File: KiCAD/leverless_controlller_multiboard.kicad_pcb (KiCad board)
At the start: 2 copper layers, 210 x 130 mm, 67 parts, among them J1 USB_C_Receptacle_USB2.0_14P, J2 Conn_01x03_Socket, SW1 Memory Reset, SW10_SHARE1 SW_Push, SW11_START1 SW_Push, SW12_THROW1 SW_Push, SW14_PS1 SW_Push, SW15_TOUCHPAD1 SW_Push, SW16_SPACE1 SW_Push, SW17_W1 SW_Push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

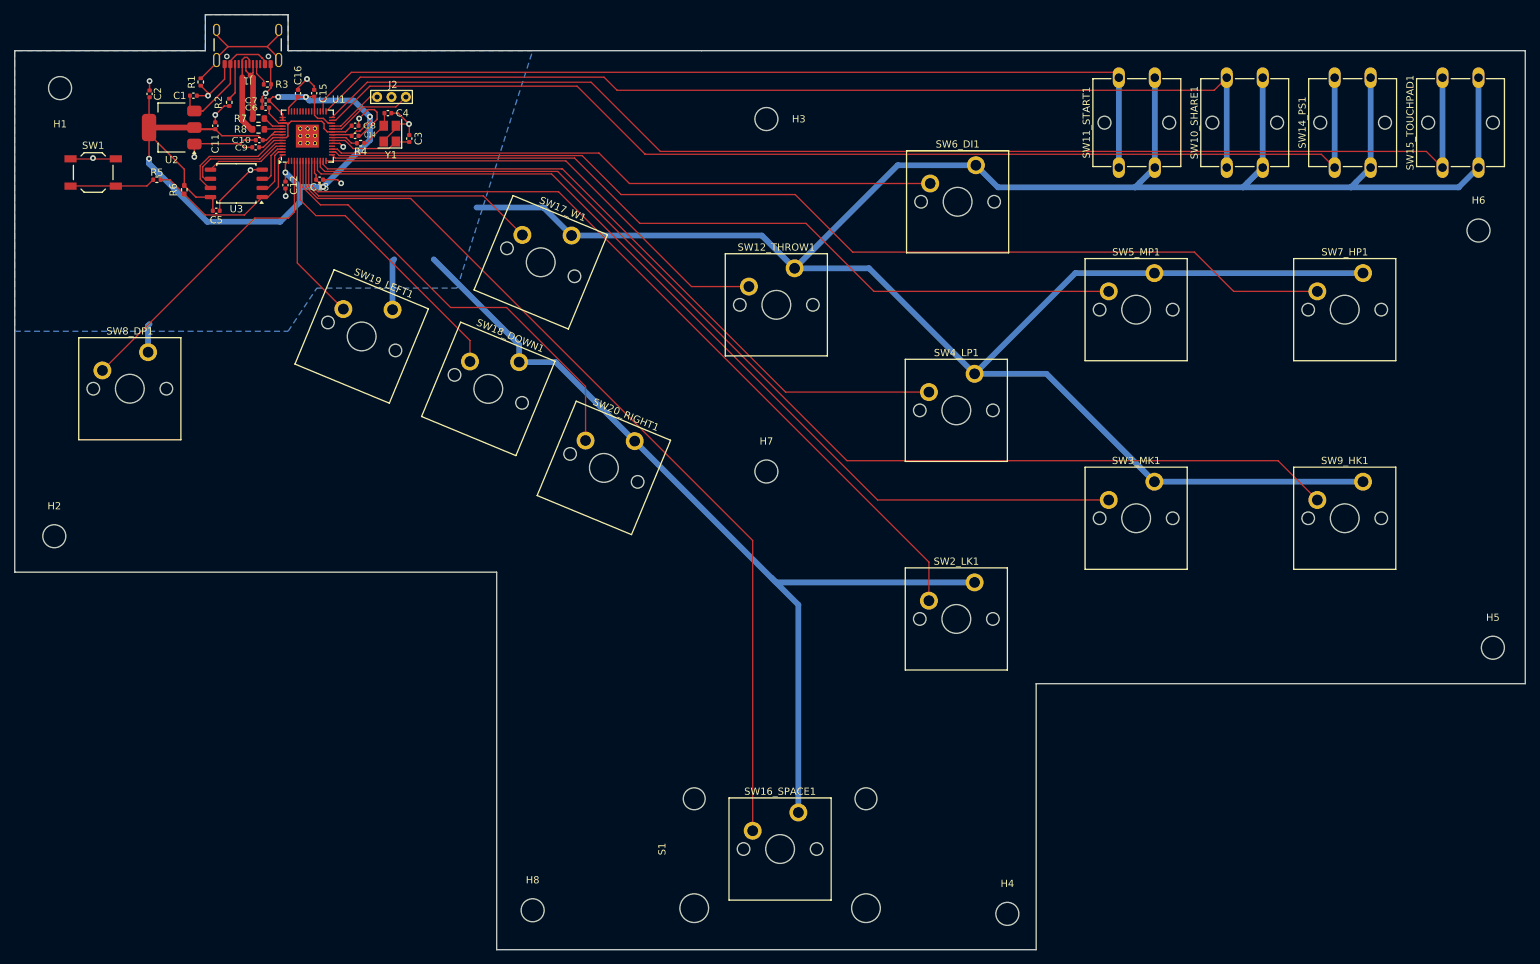
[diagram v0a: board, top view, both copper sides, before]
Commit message: Add multiboard configurations
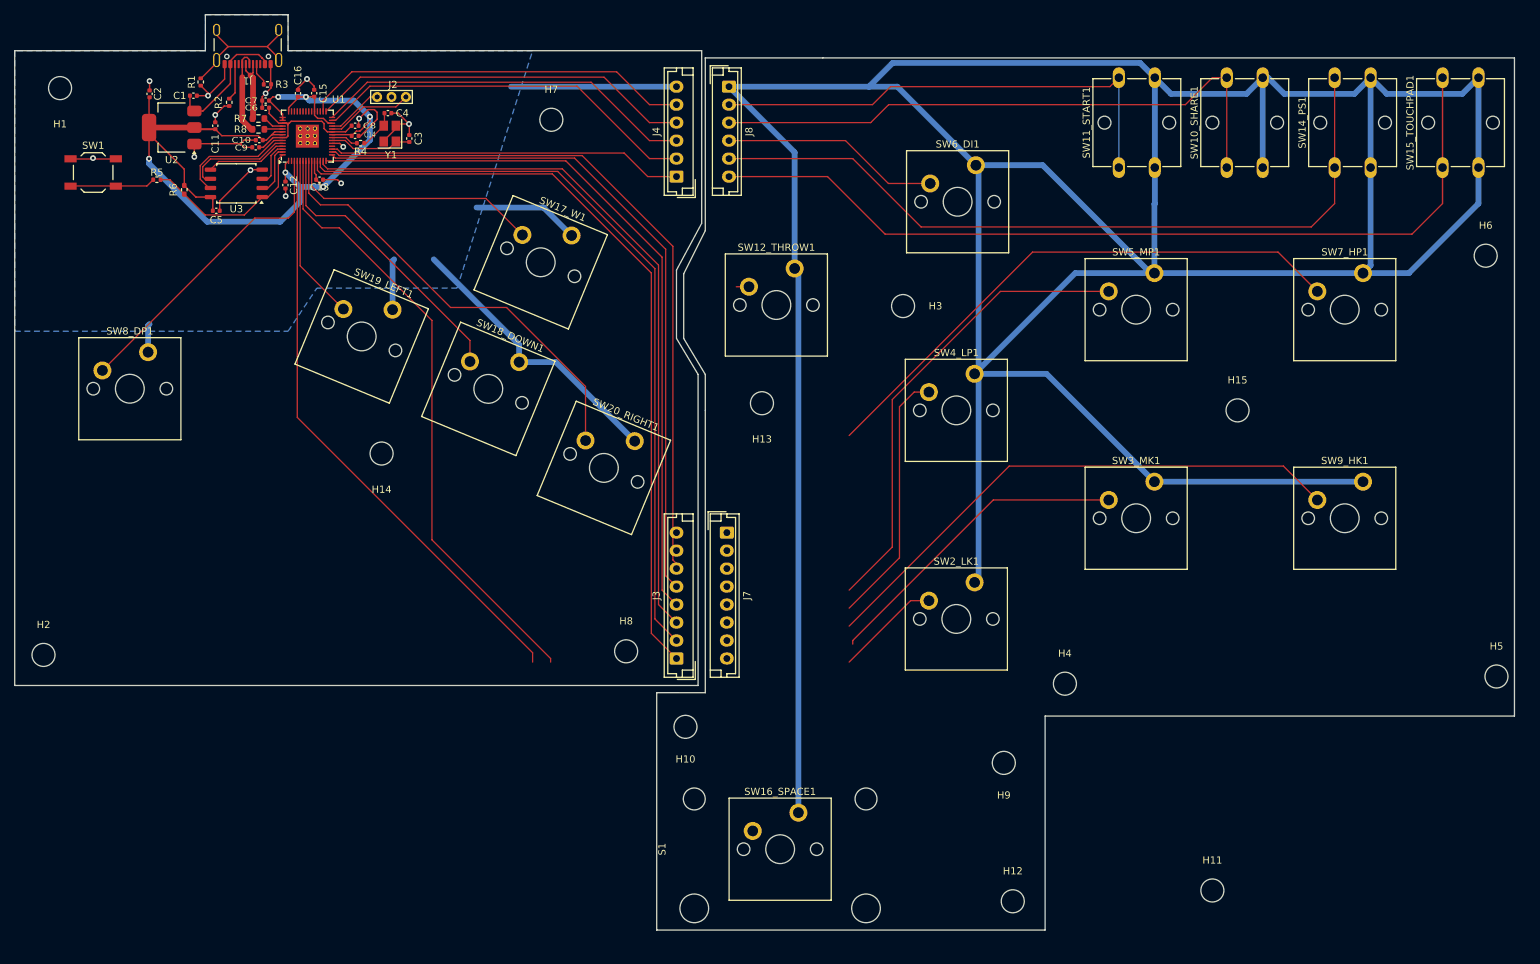
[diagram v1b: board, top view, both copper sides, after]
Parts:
- added B1: Board, PCM_kikit:Board, F.Cu at (57.0, 25.0)
- added B2: Board, PCM_kikit:Board, F.Cu at (158.5, 25.0)
- added H10: MountingHole, MountingHole:MountingHole_3.2mm_M3, F.Cu at (137.2, 119.0)
- added H11: MountingHole, MountingHole:MountingHole_3.2mm_M3, F.Cu at (210.5, 141.8)
- added H12: MountingHole, MountingHole:MountingHole_3.2mm_M3, F.Cu at (182.8, 143.2)
- added H13: MountingHole, MountingHole:MountingHole_3.2mm_M3, F.Cu at (147.9, 74.0)
- added H14: MountingHole, MountingHole:MountingHole_3.2mm_M3, F.Cu at (95.0, 81.0)
- added H15: MountingHole, MountingHole:MountingHole_3.2mm_M3, F.Cu at (214.0, 75.0)
- added H9: MountingHole, MountingHole:MountingHole_3.2mm_M3, F.Cu at (181.5, 124.0)
- added J3: Conn_01x06_Socket, Connector_JST:JST_EH_B8B-EH-A_1x08_P2.50mm_Vertical, F.Cu at (136.0, 109.5)
- added J4: Conn_01x06_Socket, Connector_JST:JST_EH_B6B-EH-A_1x06_P2.50mm_Vertical, F.Cu at (136.0, 42.5)
- added J7: Conn_01x06_Socket, Connector_JST:JST_EH_B8B-EH-A_1x08_P2.50mm_Vertical, F.Cu at (143.0, 92.0)
- added J8: Conn_01x06_Socket, Connector_JST:JST_EH_B6B-EH-A_1x06_P2.50mm_Vertical, F.Cu at (143.3, 30.0)
- C1, C2: value 10u -> 4.7u
- moved H7 57.3 mm to (118.6, 34.6)
- moved H8 38.3 mm to (129.0, 108.5)
- moved H4 33.0 mm to (190.0, 113.0)
- moved H3 32.2 mm to (167.5, 60.5)
- moved H2 16.6 mm to (48.0, 109.0)
- moved H5 4.03 mm to (250.0, 112.0)
- moved H6 3.64 mm to (248.5, 53.5)
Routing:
- net (no net): track 0.00 -> 1293.5 mm
- net A2: track 173.8 -> 0.00 mm
- net A1: track 158.5 -> 0.00 mm
- net S1: track 141.2 -> 0.00 mm
- net GND: track 580.6 -> 713.7 mm
- net S2: track 126.6 -> 0.00 mm
- net SPACE: track 126.4 -> 0.37 mm
- net B1: track 116.3 -> 14.6 mm
- net B2: track 130.3 -> 44.2 mm
- net L1: track 85.6 -> 0.00 mm
- net RIGHT: track 61.9 -> 147.0 mm
- net LEFT: track 23.3 -> 106.3 mm
- net R2: track 158.6 -> 76.3 mm
- net R1: track 145.0 -> 77.9 mm
- net L3: track 66.0 -> 1.77 mm
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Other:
- board size 210 x 130 mm -> 208.5 x 127.2 mm
